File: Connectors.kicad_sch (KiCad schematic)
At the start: 3 parts, among them J1 GD820HTX75P6HB, J2 2-338069-0

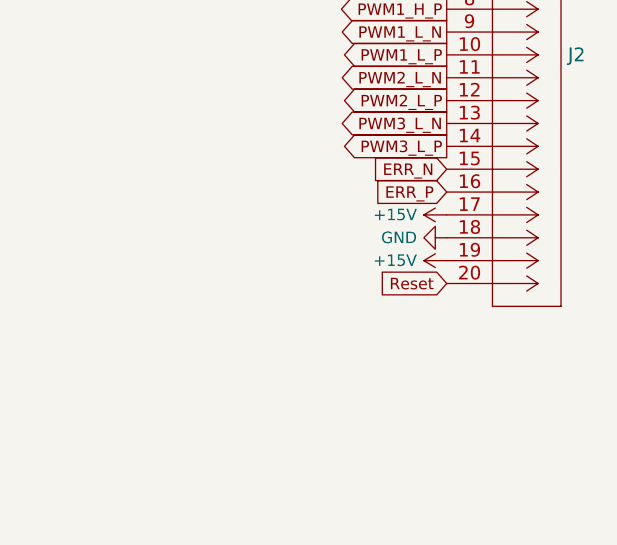
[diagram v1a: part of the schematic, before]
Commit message: Изменил схему
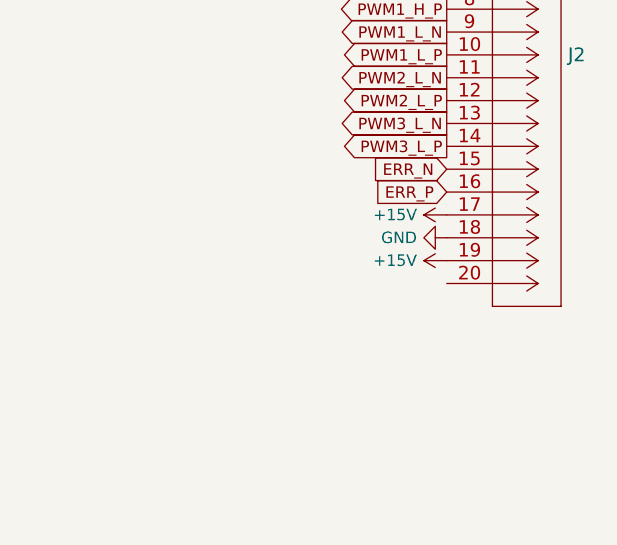
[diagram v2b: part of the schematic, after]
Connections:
- net Reset: no longer names the net of J2.20

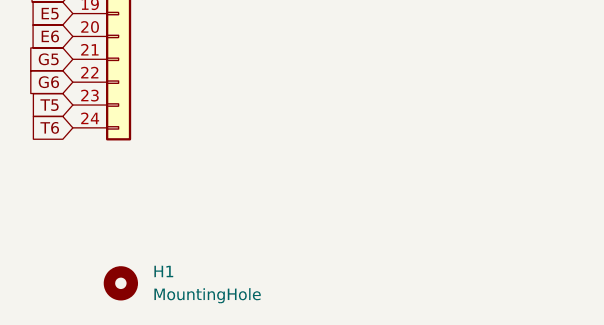
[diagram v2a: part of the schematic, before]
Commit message: Разместил все три стойки в своей области
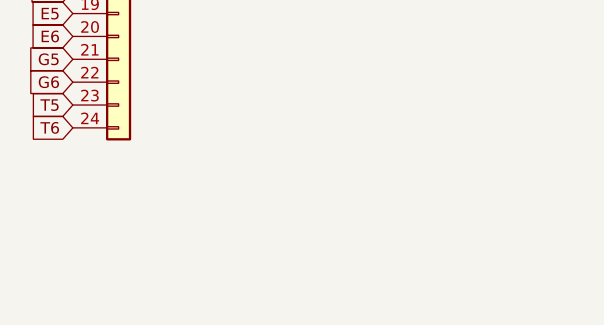
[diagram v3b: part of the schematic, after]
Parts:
- removed H1: MountingHole, MountingHole:MountingHole_3.2mm_M3, symbol Mechanical:MountingHole
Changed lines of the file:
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@@
-	)
-	(symbol
-		(lib_id "Mechanical:MountingHole")
-		(at 33.274 106.68 0)
-		(unit 1)
-		(exclude_from_sim no)
-		(in_bom yes)
-		(on_board yes)
-		(dnp no)
-		(fields_autoplaced yes)
-		(property "Reference" "H1"
-			(at 36.83 105.4099 0)
-			(effects
-				(font
-					(size 1.27 1.27)
-				)
-				(justify left)
-			)
-		)
-		(property "Value" "MountingHole"
-			(at 36.83 107.9499 0)
-			(effects
-				(font
-					(size 1.27 1.27)
-				)
-				(justify left)
-			)
-		)
-		(property "Footprint" "MountingHole:MountingHole_3.2mm_M3"
-			(at 33.274 106.68 0)
-			(effects
-				(font
-					(size 1.27 1.27)
-				)
-				(hide yes)
-			)
-		)
-		(property "Datasheet" "~"
-			(at 33.274 106.68 0)
-			(effects
-				(font
-					(size 1.27 1.27)
-				)
-				(hide yes)
-			)
-		)
-		(property "Description" ""
-			(at 33.274 106.68 0)
-			(effects
-				(font
-					(size 1.27 1.27)
-				)
-				(hide yes)
-			)
-		)
-		(instances
-			(project "Adapter"
-				(path "/e63e39d7-6ac0-4ffd-8aa3-1841a4541b55/98be4b32-51d8-4f7b-9b74-14890e40923b"
-					(reference "H1")
-					(unit 1)
-				)
-			)
-		)
 	)
 	(symbol

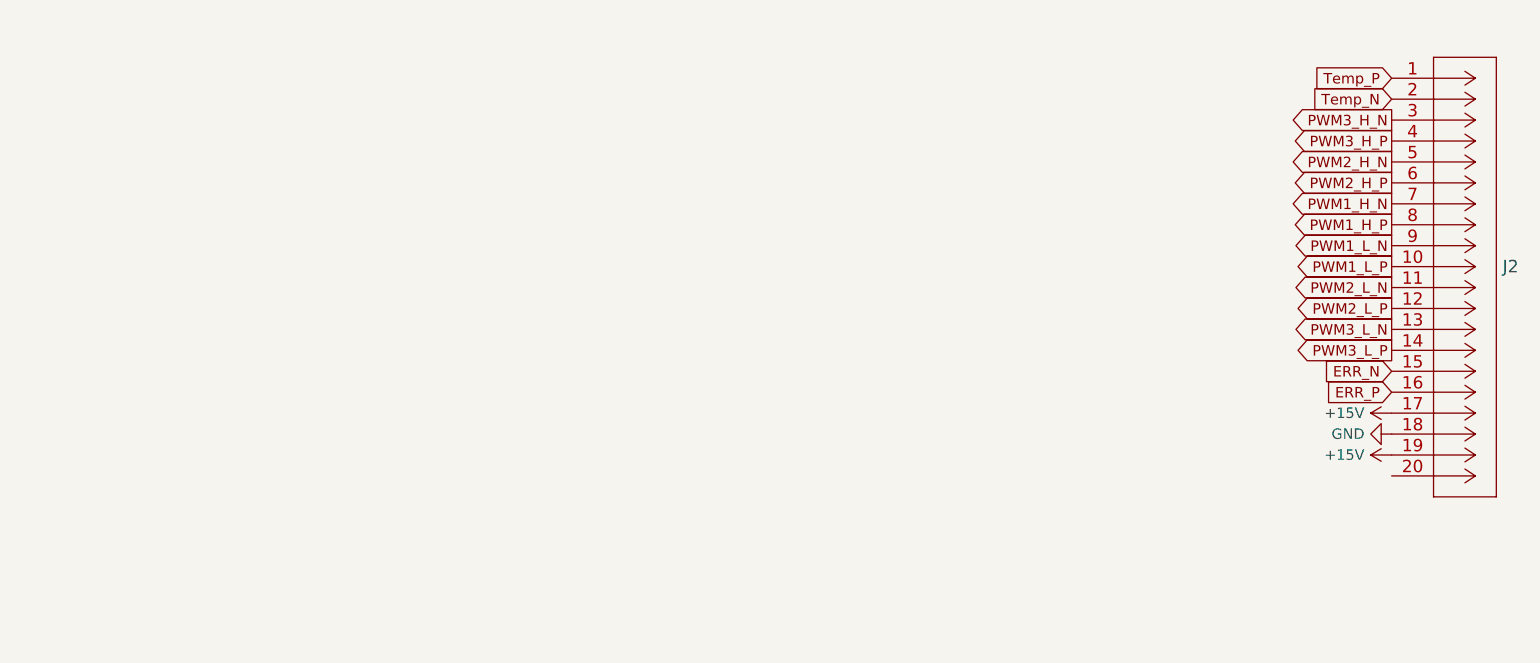
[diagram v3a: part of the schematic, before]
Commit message: Добавил новые разъёмы
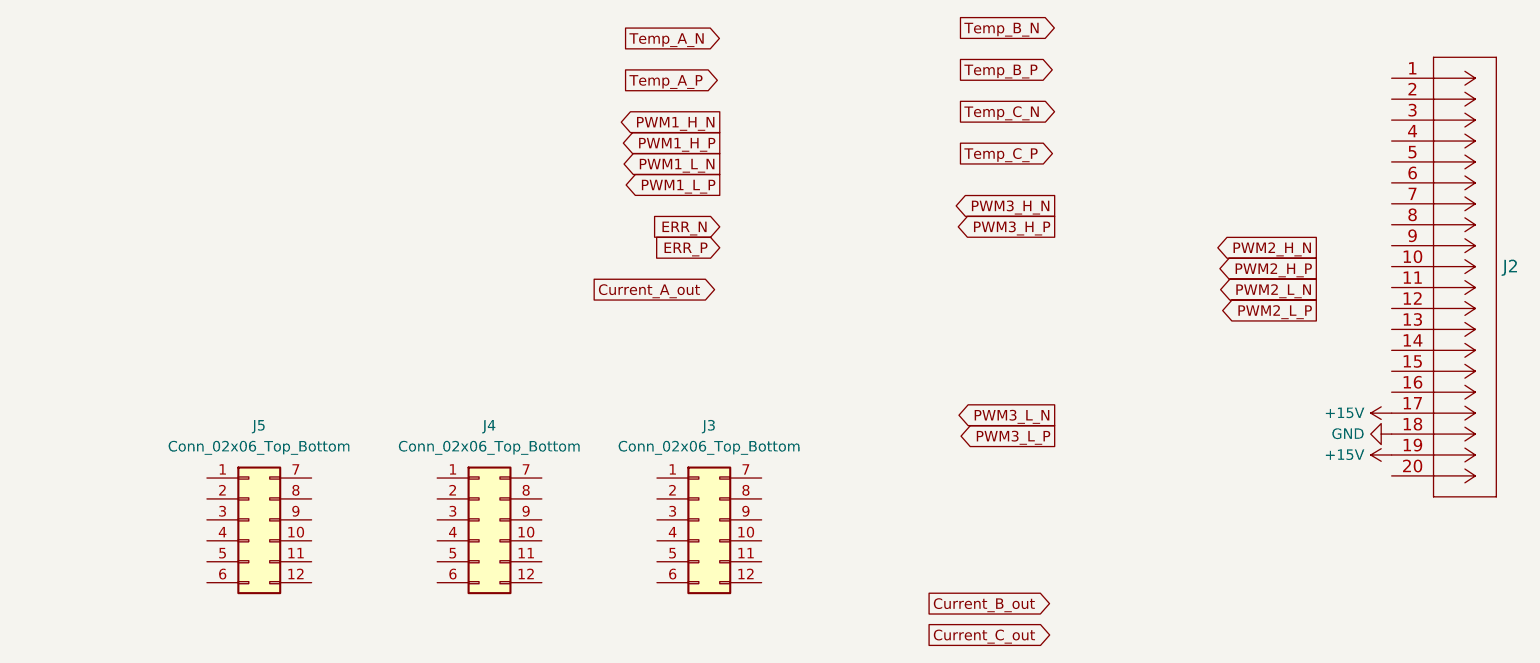
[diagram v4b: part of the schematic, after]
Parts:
- added J3, J4, J5: Conn_02x06_Top_Bottom, Connector_Molex:Molex_Micro-Fit_3.0_43045-1212_2x06_P3.00mm_Vertical, symbol Connector_Generic:Conn_02x06_Top_Bottom
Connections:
- net ERR_N: no longer J2.15
- net ERR_P: no longer J2.16
- net PWM1_H_N: no longer J2.7
- net PWM1_H_P: no longer J2.8
- net PWM1_L_N: no longer J2.9
- net PWM1_L_P: no longer J2.10
- net PWM2_H_N: no longer J2.5
- net PWM2_H_P: no longer J2.6
- net PWM2_L_N: no longer J2.11
- net PWM2_L_P: no longer J2.12
- net PWM3_H_N: no longer J2.3
- net PWM3_H_P: no longer J2.4
- net PWM3_L_N: no longer J2.13
- net PWM3_L_P: no longer J2.14
- net Temp_N: no longer names the net of J2.2
- net Temp_P: no longer names the net of J2.1

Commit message: Развел вторую стойку
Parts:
- removed J2: 2-338069-0, Connector_My:2-338069-0, symbol Connector_My:2-338069-0
- J3: renamed from J5; value Conn_02x06_Top_Bottom -> Control_A
- J4: renamed from J3; value Conn_02x06_Top_Bottom -> Control_C
- J5: renamed from J4; value Conn_02x06_Top_Bottom -> Control_B
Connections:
- net +15V: now also J3.7 (Pin_7), J4.7 (Pin_7), J5.7 (Pin_7)
- net Current_A_out: now also J3.10 (Pin_10)
- net Current_B_out: now also J5.10 (Pin_10)
- net Current_C_out: now also J4.10 (Pin_10)
- net GND: now also J3.1 (Pin_1), J4.1 (Pin_1), J5.1 (Pin_1)
- net PWM1_H_N: now also J3.5 (Pin_5)
- net PWM1_H_P: now also J3.11 (Pin_11)
- net PWM1_L_N: now also J3.2 (Pin_2)
- net PWM1_L_P: now also J3.8 (Pin_8)
- net PWM2_H_N: now also J5.5 (Pin_5)
- net PWM2_H_P: now also J5.11 (Pin_11)
- net PWM2_L_N: now also J5.2 (Pin_2)
- net PWM2_L_P: now also J5.8 (Pin_8)
- net PWM3_H_N: now also J4.5 (Pin_5)
- net PWM3_H_P: now also J4.11 (Pin_11)
- net PWM3_L_N: now also J4.2 (Pin_2)
- net PWM3_L_P: now also J4.8 (Pin_8)
- net Temp_A_N: now also J3.9 (Pin_9)
- net Temp_A_P: now also J3.3 (Pin_3)
- net Temp_B_N: now also J5.9 (Pin_9)
- net Temp_B_P: now also J5.3 (Pin_3)
- net Temp_C_N: now also J4.9 (Pin_9)
- net Temp_C_P: now also J4.3 (Pin_3)
- net ERR_C_N: now reaches J4.12 (Pin_12)
- net ~{RST}: now reaches J4.4 (Pin_4)
- net ~{RST}: now also J3.4 (Pin_4), J5.4 (Pin_4)
- net ERR_C_P: now reaches J4.6 (Pin_6)
- net ERR_A_N: now reaches J3.12 (Pin_12)
- net ERR_A_P: now reaches J3.6 (Pin_6)
- net ERR_B_N: now reaches J5.12 (Pin_12)
- net ERR_B_P: now reaches J5.6 (Pin_6)
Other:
- moved on the sheet: J3, J4, J5

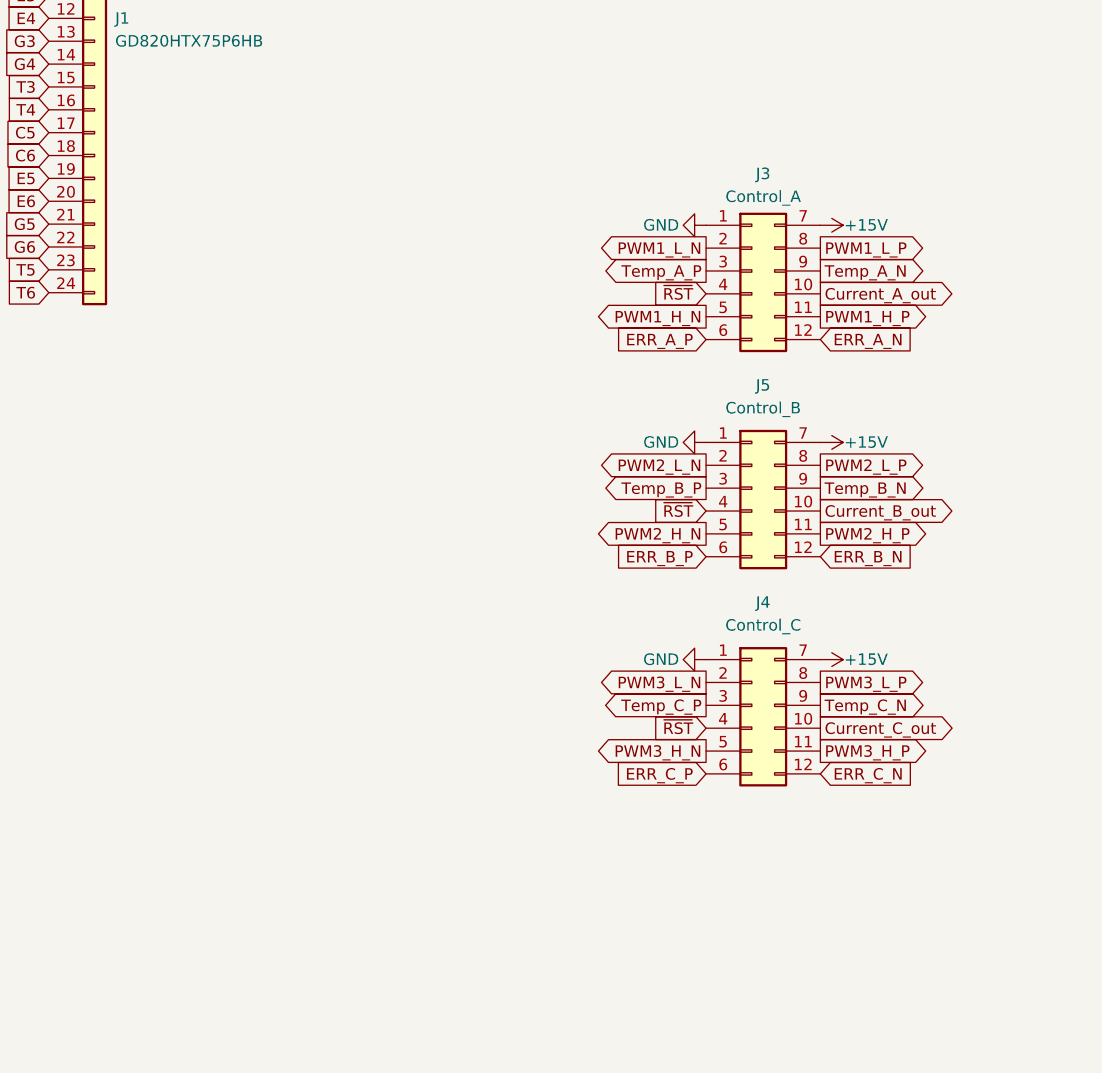
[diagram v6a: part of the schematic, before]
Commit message: Отправил на проверку в резонит: изменил BOM
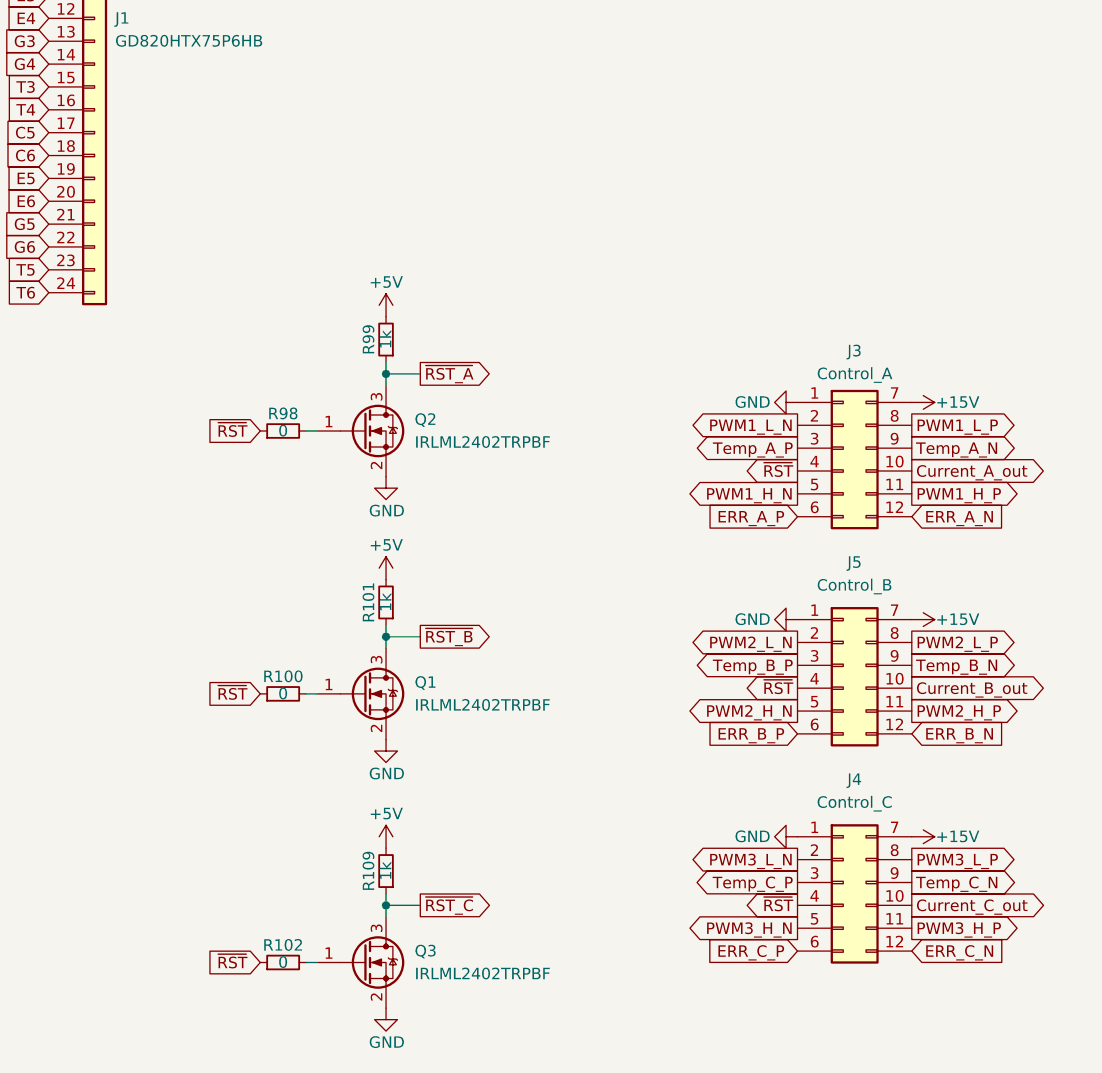
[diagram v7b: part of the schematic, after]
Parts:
- added Q1, Q2, Q3: IRLML2402TRPBF, Package_TO_SOT_SMD:SOT-23, symbol Transistor_FET:2N7002
- added R100, R102, R98: 0, Resistor_SMD:R_0805_2012Metric_Pad1.20x1.40mm_HandSolder, symbol Device:R_Small
- added R101, R109, R99: 1k, Resistor_SMD:R_0805_2012Metric_Pad1.20x1.40mm_HandSolder, symbol Device:R_Small
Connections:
- net GND: now also Q1.2 (S), Q2.2 (S), Q3.2 (S)
- net ~{RST}: now also R100.1, R102.1, R98.1
- new net: Q3.1 (G), R102.2
- new net: Q1.1 (G), R100.2
- new net: Q2.1 (G), R98.2
- new net +5V: R101.2, R109.2, R99.2
- new net ~{RST_A}: Q2.3 (D), R99.1
- new net ~{RST_B}: Q1.3 (D), R101.1
- new net ~{RST_C}: Q3.3 (D), R109.1
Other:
- moved on the sheet: J3, J4, J5
